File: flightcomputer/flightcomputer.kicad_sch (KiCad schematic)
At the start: 73 parts, among them J1 Conn_Coaxial, J10 Conn_01x03, J11 Conn_01x03, J12 ESQ-113-14-G-D, J13 Conn_01x07, J14 S3B-PH-K-S-GW, J2 Conn_Coaxial, J3 Conn_Coaxial, J4 Conn_Coaxial, J5 S3B-PH-K-S-GW, J6 Conn_01x03, J7 S4B-PH-K-S_LF__SN_, J8 Conn_01x03, J9 Conn_01x06, U1 MAX-M10S, U2 LIS2MDLTR, U3 BMI088, U4 MS5607-02BA, U5 ESP32-S3-WROOM-1-N4, U7 Teensy4.1, U8 LSM6DSO32TR, U9 RFM96W-433S2

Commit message: fixes
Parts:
- added S2: EG1218, HPRlibrary:SW_EG1218, symbol HPRlibrary:EG1218
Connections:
- net radio_miso: now also U9.2 (MISO); no longer U9.3 (MOSI)
- net radio_mosi: now also U9.3 (MOSI); no longer U9.2 (MISO)
- net teensy_3.3v: now also S2.2; no longer C10.1, U9.13 (3.3V)
- new net radio_3.3v: C10.1, S2.3, U9.13 (3.3V)
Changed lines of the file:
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@@
 	(wire
 		(pts
+			(xy 266.7 217.17) (xy 279.4 217.17)
+		)
+		(stroke
+			(width 0)
+			(type default)
+		)
+	)
+	(wire
+		(pts
 			(xy 372.11 220.98) (xy 373.38 220.98)
 		)
@@
 	(wire
 		(pts
+			(xy 266.7 214.63) (xy 279.4 214.63)
+		)
+		(stroke
+			(width 0)
+			(type default)
+		)
+	)
+	(wire
+		(pts
 			(xy 321.31 62.23) (xy 321.31 72.39)
 		)
@@
 		)
 	)
-	(label "teensy_3.3v"
+	(label "radio_3.3v"
 		(at 233.68 233.68 0)
 		(effects
@@
 		)
 	)
-	(label "radio_mosi"
+	(label "radio_miso"
 		(at 186.69 254 0)
 		(effects
@@
 		)
 	)
-	(label "radio_miso"
+	(label "radio_mosi"
 		(at 186.69 256.54 0)
 		(effects
@@
 		)
 	)
+	(label "teensy_3.3v"
+		(at 266.7 214.63 0)
+		(effects
+			(font
+				(size 1.27 1.27)
+			)
+			(justify left bottom)
+		)
+	)
 	(label "mag_cs"
 		(at 240.03 160.02 180)
@@
 		)
 	)
+	(label "radio_3.3v"
+		(at 266.7 217.17 0)
+		(effects
+			(font
+				(size 1.27 1.27)
+			)
+			(justify left bottom)
+		)
+	)
 	(label "imu_accel_int1"
 		(at 205.74 55.88 180)
@@
 					(unit 1)
 				)
+			)
+		)
+	)
+	(symbol
+		(lib_id "HPRlibrary:EG1218")
+		(at 284.48 214.63 0)
+		(unit 1)
+		(exclude_from_sim no)
+		(in_bom yes)
+		(on_board yes)
+		(dnp no)
+		(fields_autoplaced yes)
+		(property "Reference" "S2"
+			(at 288.29 213.3599 0)
+			(effects
+				(font
+					(size 1.27 1.27)
+				)
+				(justify left)
+			)
+		)
+		(property "Value" "EG1218"
+			(at 288.29 215.8999 0)
+			(effects
+				(font
+					(size 1.27 1.27)
+				)
+				(justify left)
+			)
+		)
+		(property "Footprint" "HPRlibrary:SW_EG1218"
+			(at 284.48 214.63 0)
+			(effects
+				(font
+					(size 1.27 1.27)
+				)
+				(justify bottom)
+				(hide yes)
+			)
+		)
+		(property "Datasheet" ""
+			(at 284.48 214.63 0)
+			(effects
+				(font
+					(size 1.27 1.27)
+				)
+				(hide yes)
+			)
+		)
+		(property "Description" "Slide Switch SPDT Through Hole"
+			(at 284.48 214.63 0)
+			(effects
+				(font
+					(size 1.27 1.27)
+				)
+				(justify bottom)
+				(hide yes)
+			)
+		)
+		(property "MF" "E-Switch"
+			(at 284.48 214.63 0)
+			(effects
+				(font
+					(size 1.27 1.27)
+				)
+				(justify bottom)
+				(hide yes)
+			)
+		)
+		(property "PACKAGE" "None"
+			(at 284.48 214.63 0)
+			(effects
+				(font
+					(size 1.27 1.27)
+				)
+				(justify bottom)
+				(hide yes)
+			)
+		)
+		(property "PRICE" "None"
+			(at 284.48 214.63 0)
+			(effects
+				(font
+					(size 1.27 1.27)
+				)
+				(justify bottom)
+				(hide yes)
+			)
+		)
+		(property "MP" "EG1218"
+			(at 284.48 214.63 0)
+			(effects
+				(font
+					(size 1.27 1.27)
+				)
+				(justify bottom)
+				(hide yes)
+			)
+		)
+		(property "AVAILABILITY" "In Stock"
+			(at 284.48 214.63 0)
+			(effects
+				(font
+					(size 1.27 1.27)
+				)
+				(justify bottom)
+				(hide yes)
+			)
+		)
+		(property "PURCHASE-URL" "https://pricing.snapeda.com/search/part/EG1218/?ref=eda"
+			(at 284.48 214.63 0)
+			(effects
+				(font
+					(size 1.27 1.27)
+				)
+				(justify bottom)
+				(hide yes)
+			)
+		)
+		(pin "1"
+		)
+		(pin "2"
+		)
+		(pin "3"
+		)
+		(instances
+			(project "flightcomputer"
+				(path "/7ffad011-bb39-4f19-b4f2-0143f1626449"
+					(reference "S2")
+					(unit 1)
+				)

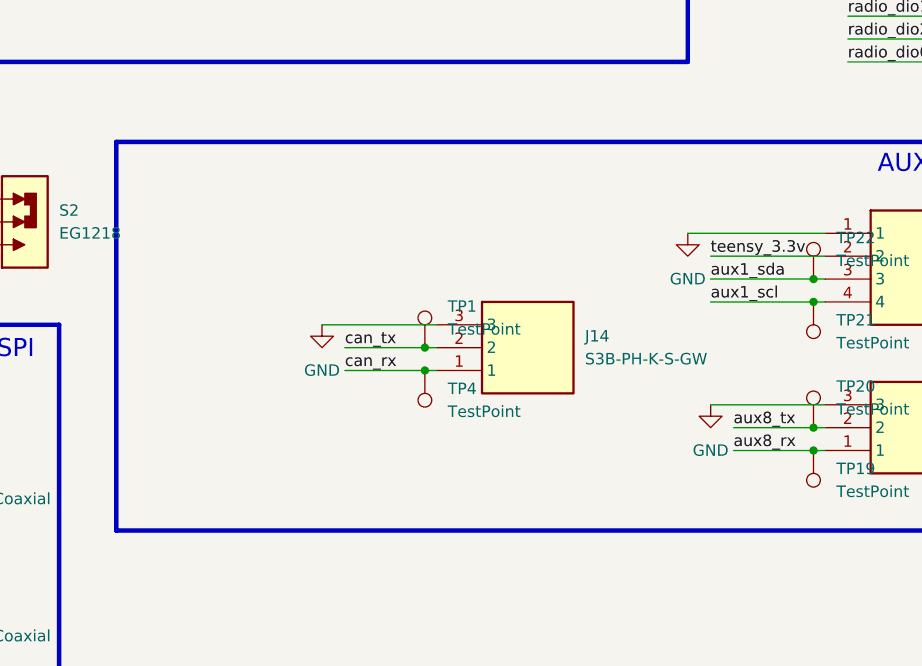
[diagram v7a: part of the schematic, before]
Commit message: add jst 2pin for 5V fc
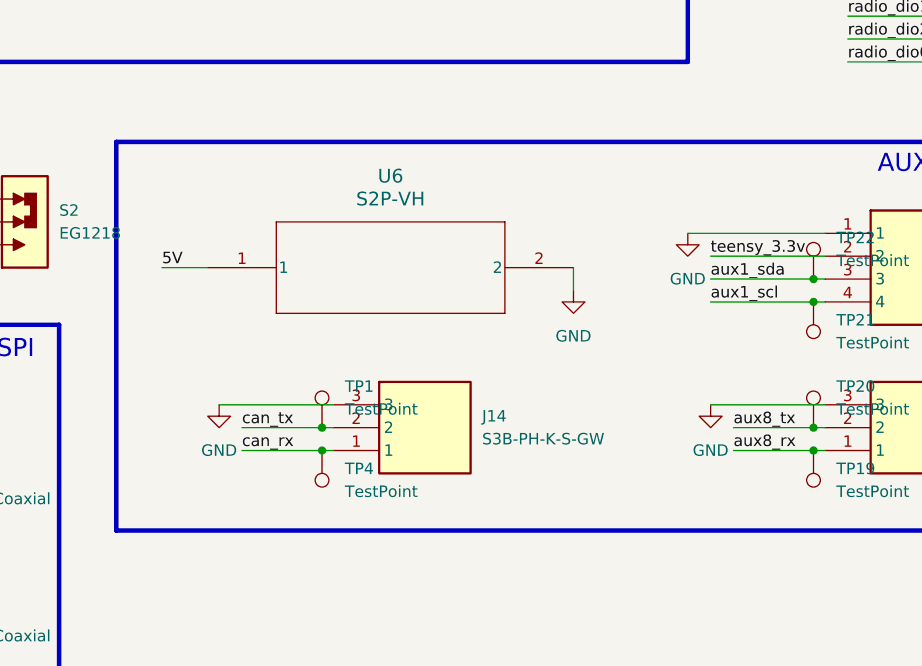
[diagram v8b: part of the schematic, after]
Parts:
- added U6: S2P-VH, S2P-VH_JST, symbol HPRsymbols:S2P-VH
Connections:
- net 5V: now also U6.1
- net GND: now also U6.2
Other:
- moved on the sheet: J14, TP1, TP4
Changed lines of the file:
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@@
 	)
 	(junction
-		(at 328.93 228.6)
+		(at 317.5 237.49)
 		(diameter 0)
 		(color 0 0 0 0)
@@
 	)
 	(junction
-		(at 328.93 231.14)
+		(at 317.5 240.03)
 		(diameter 0)
 		(color 0 0 0 0)
@@
 	(wire
 		(pts
-			(xy 320.04 228.6) (xy 328.93 228.6)
+			(xy 308.61 237.49) (xy 317.5 237.49)
 		)
 		(stroke
@@
 	(wire
 		(pts
-			(xy 328.93 228.6) (xy 330.2 228.6)
+			(xy 317.5 237.49) (xy 318.77 237.49)
 		)
 		(stroke
@@
 	(wire
 		(pts
-			(xy 328.93 231.14) (xy 330.2 231.14)
+			(xy 317.5 240.03) (xy 318.77 240.03)
 		)
 		(stroke
@@
 	(wire
 		(pts
-			(xy 317.5 226.06) (xy 330.2 226.06)
+			(xy 306.07 234.95) (xy 318.77 234.95)
 		)
 		(stroke
@@
 	(wire
 		(pts
-			(xy 320.04 231.14) (xy 328.93 231.14)
+			(xy 308.61 240.03) (xy 317.5 240.03)
+		)
+		(stroke
+			(width 0)
+			(type default)
+		)
+	)
+	(wire
+		(pts
+			(xy 299.72 219.71) (xy 304.8 219.71)
 		)
 		(stroke
@@
 	(wire
 		(pts
+			(xy 345.44 222.25) (xy 345.44 219.71)
+		)
+		(stroke
+			(width 0)
+			(type default)
+		)
+	)
+	(wire
+		(pts
 			(xy 300.99 69.85) (xy 300.99 72.39)
 		)
@@
 		)
 	)
+	(label "5V"
+		(at 299.72 219.71 0)
+		(effects
+			(font
+				(size 1.27 1.27)
+			)
+			(justify left bottom)
+		)
+	)
 	(label "gps_vbckp"
 		(at 130.81 250.19 0)
@@
 	)
 	(label "can_rx"
-		(at 320.04 231.14 0)
+		(at 308.61 240.03 0)
 		(effects
 			(font
@@
 	)
 	(label "can_tx"
-		(at 320.04 228.6 0)
+		(at 308.61 237.49 0)
 		(effects
 			(font
@@
 	(symbol
 		(lib_id "power:GND")
+		(at 345.44 222.25 0)
+		(unit 1)
+		(exclude_from_sim no)
+		(in_bom yes)
+		(on_board yes)
+		(dnp no)
+		(fields_autoplaced yes)
+		(property "Reference" "#PWR033"
+			(at 345.44 228.6 0)
+			(effects
+				(font
+					(size 1.27 1.27)
+				)
+				(hide yes)
+			)
+		)
+		(property "Value" "GND"
+			(at 345.44 227.33 0)
+			(effects
+				(font
+					(size 1.27 1.27)
+				)
+			)
+		)
+		(property "Footprint" ""
+			(at 345.44 222.25 0)
+			(effects
+				(font
+					(size 1.27 1.27)
+				)
+				(hide yes)
+			)
+		)
+		(property "Datasheet" ""
+			(at 345.44 222.25 0)
+			(effects
+				(font
+					(size 1.27 1.27)
+				)
+				(hide yes)
+			)
+		)
+		(property "Description" "Power symbol creates a global label with name \"GND\" , ground"
+			(at 345.44 222.25 0)
+			(effects
+				(font
+					(size 1.27 1.27)
+				)
+				(hide yes)
+			)
+		)
+		(pin "1"
+		)
+		(instances
+			(project "flightcomputer"
+				(path "/7ffad011-bb39-4f19-b4f2-0143f1626449"
+					(reference "#PWR033")
+					(unit 1)
+				)
+			)
+		)
+	)
+	(symbol
+		(lib_id "power:GND")
 		(at 566.42 184.15 0)
 		(unit 1)
@@
 	(symbol
 		(lib_id "Connector:TestPoint")
-		(at 328.93 231.14 180)
+		(at 317.5 240.03 180)
 		(unit 1)
 		(exclude_from_sim no)
@@
 		(fields_autoplaced yes)
 		(property "Reference" "TP4"
-			(at 331.47 233.1719 0)
+			(at 320.04 242.0619 0)
 			(effects
 				(font
@@
 		)
 		(property "Value" "TestPoint"
-			(at 331.47 235.7119 0)
+			(at 320.04 244.6019 0)
 			(effects
 				(font
@@
 		)
 		(property "Footprint" "Connector_PinHeader_2.54mm:PinHeader_1x01_P2.54mm_Vertical"
-			(at 323.85 231.14 0)
+			(at 312.42 240.03 0)
 			(effects
 				(font
@@
 		)
 		(property "Datasheet" "~"
-			(at 323.85 231.14 0)
+			(at 312.42 240.03 0)
 			(effects
 				(font
@@
 		)
 		(property "Description" "test point"
-			(at 328.93 231.14 0)
+			(at 317.5 240.03 0)
 			(effects
 				(font
@@
 	)
 	(symbol
+		(lib_id "HPRsymbols:S2P-VH")
+		(at 304.8 219.71 0)
+		(unit 1)
+		(exclude_from_sim no)
+		(in_bom yes)
+		(on_board yes)
+		(dnp no)
+		(fields_autoplaced yes)
+		(property "Reference" "U6"
+			(at 325.12 209.55 0)
+			(effects
+				(font
+					(size 1.524 1.524)
+				)
+			)
+		)
+		(property "Value" "S2P-VH"
+			(at 325.12 212.09 0)
+			(effects
+				(font
+					(size 1.524 1.524)
+				)
+			)
+		)
+		(property "Footprint" "S2P-VH_JST"
+			(at 304.8 219.71 0)
+			(effects
+				(font
+					(size 1.27 1.27)
+					(italic yes)
+				)
+				(hide yes)
+			)
+		)
+		(property "Datasheet" "S2P-VH"
+			(at 304.8 219.71 0)
+			(effects
+				(font
+					(size 1.27 1.27)
+					(italic yes)
+				)
+				(hide yes)
+			)
+		)
+		(property "Description" ""
+			(at 304.8 219.71 0)
+			(effects
+				(font
+					(size 1.27 1.27)
+				)
+				(hide yes)
+			)
+		)
+		(pin "2"
+		)
+		(pin "1"
+		)
+		(instances
+			(project ""
+				(path "/7ffad011-bb39-4f19-b4f2-0143f1626449"
+					(reference "U6")
+					(unit 1)
+				)
+			)
+		)
+	)
+	(symbol
 		(lib_id "HPRlibrary:S4B-PH-K-S_LF__SN_")
 		(at 373.38 215.9 0)
@@
 	(symbol
 		(lib_id "Connector:TestPoint")
-		(at 328.93 228.6 0)
+		(at 317.5 237.49 0)
 		(unit 1)
 		(exclude_from_sim no)
@@
 		(fields_autoplaced yes)
 		(property "Reference" "TP1"
-			(at 331.47 224.0279 0)
+			(at 320.04 232.9179 0)
 			(effects
 				(font
@@
 		)
 		(property "Value" "TestPoint"
-			(at 331.47 226.5679 0)
+			(at 320.04 235.4579 0)
 			(effects
 				(font
@@
 		)
 		(property "Footprint" "Connector_PinHeader_2.54mm:PinHeader_1x01_P2.54mm_Vertical"
-			(at 334.01 228.6 0)
+			(at 322.58 237.49 0)
 			(effects
 				(font
@@
 		)
 		(property "Datasheet" "~"
-			(at 334.01 228.6 0)
+			(at 322.58 237.49 0)
 			(effects
 				(font
@@
 		)
 		(property "Description" "test point"
-			(at 328.93 228.6 0)
+			(at 317.5 237.49 0)
 			(effects
 				(font
@@
 	(symbol
 		(lib_id "power:GND")
-		(at 317.5 226.06 0)
+		(at 306.07 234.95 0)
 		(unit 1)
 		(exclude_from_sim no)
@@
 		(fields_autoplaced yes)
 		(property "Reference" "#PWR029"
-			(at 317.5 232.41 0)
+			(at 306.07 241.3 0)
 			(effects
 				(font
@@
 		)
 		(property "Value" "GND"
-			(at 317.5 231.14 0)
+			(at 306.07 240.03 0)
 			(effects
 				(font
@@
 		)
 		(property "Footprint" ""
-			(at 317.5 226.06 0)
+			(at 306.07 234.95 0)
 			(effects
 				(font
@@
 		)
 		(property "Datasheet" ""
-			(at 317.5 226.06 0)
+			(at 306.07 234.95 0)
 			(effects
 				(font
@@
 		)
 		(property "Description" "Power symbol creates a global label with name \"GND\" , ground"
-			(at 317.5 226.06 0)
+			(at 306.07 234.95 0)
 			(effects
 				(font
@@
 	(symbol
 		(lib_id "HPRlibrary:S3B-PH-K-S-GW")
-		(at 330.2 226.06 0)
+		(at 318.77 234.95 0)
 		(unit 1)
 		(exclude_from_sim no)
@@
 		(fields_autoplaced yes)
 		(property "Reference" "J14"
-			(at 346.71 227.3299 0)
+			(at 335.28 236.2199 0)
 			(effects
 				(font
@@
 		)
 		(property "Value" "S3B-PH-K-S-GW"
-			(at 346.71 229.8699 0)
+			(at 335.28 238.7599 0)
 			(effects
 				(font
@@
 		)
 		(property "Footprint" "HPRlibrary:S3BPHKSGW"
-			(at 346.71 320.98 0)
+			(at 335.28 329.87 0)
 			(effects
 				(font
@@
 		)
 		(property "Datasheet" "https://www.jst-mfg.com/product/pdf/eng/ePH.pdf"
-			(at 346.71 420.98 0)
+			(at 335.28 429.87 0)
 			(effects
 				(font
@@
 		)
 		(property "Description" "Connector Header Through Hole, Right Angle 3 position 0.079\" (2.00mm)"
-			(at 330.2 226.06 0)
+			(at 318.77 234.95 0)
 			(effects
 				(font
@@
 		)
 		(property "Height" "4.8"
-			(at 346.71 620.98 0)
+			(at 335.28 629.87 0)
 			(effects
 				(font
@@
 		)
 		(property "Mouser Part Number" "306-S3B-PH-K-S-GW"
-			(at 346.71 720.98 0)
+			(at 335.28 729.87 0)
 			(effects
 				(font
@@
 		)
 		(property "Mouser Price/Stock" "https://www.mouser.co.uk/ProductDetail/JST-Commercial/S3B-PH-K-S-GW?qs=QpmGXVUTftELXF4WxsGzCQ%3D%3D"
-			(at 346.71 820.98 0)
+			(at 335.28 829.87 0)
 			(effects
 				(font
@@
 		)
 		(property "Manufacturer_Name" "JST (JAPAN SOLDERLESS TERMINALS)"
-			(at 346.71 920.98 0)
+			(at 335.28 929.87 0)
 			(effects
 				(font
@@
 		)
 		(property "Manufacturer_Part_Number" "S3B-PH-K-S-GW"
-			(at 346.71 1020.98 0)
+			(at 335.28 1029.87 0)
 			(effects
 				(font
